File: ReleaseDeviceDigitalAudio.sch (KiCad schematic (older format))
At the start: 7 parts, among them J1 Conn_02x08_Counter_Clockwise

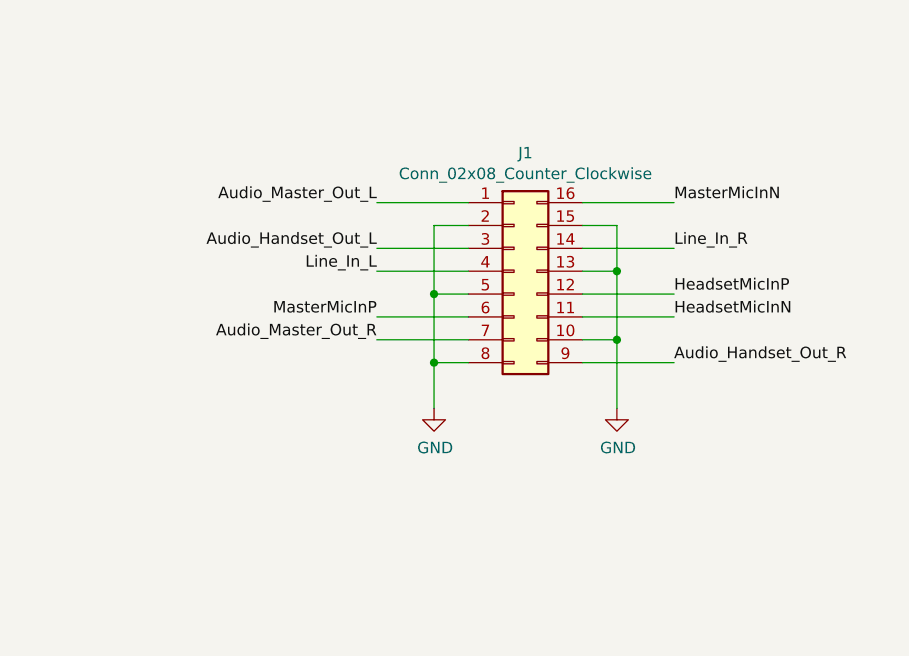
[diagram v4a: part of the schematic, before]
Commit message: - auf 20pol Audiostecker umgebaut
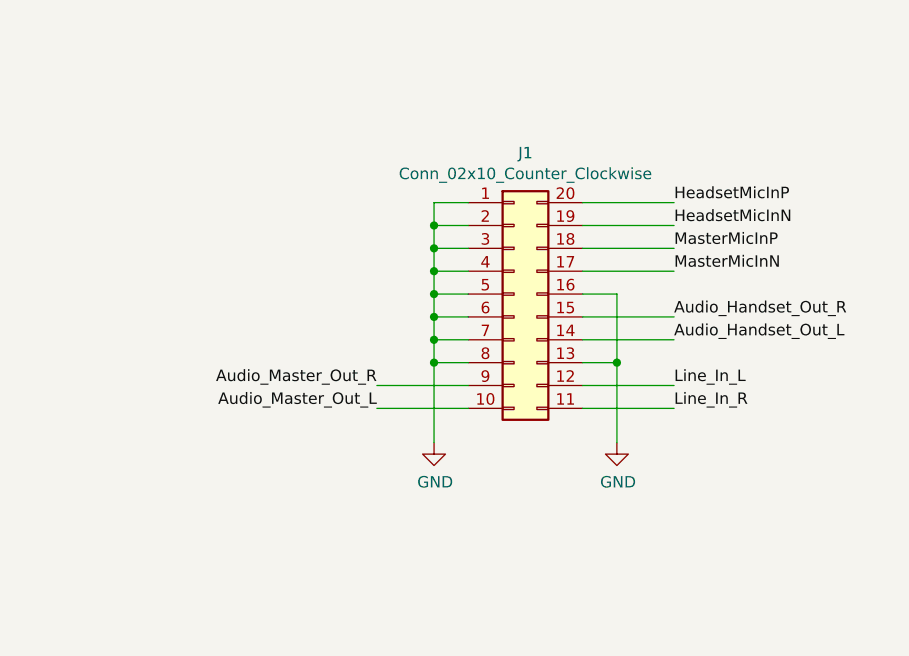
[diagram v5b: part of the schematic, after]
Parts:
- removed J1: Conn_02x08_Counter_Clockwise, TeKaDe:Molex_34825-0160, symbol Connector_Generic:Conn_02x08_Counter_Clockwise
- added J1: Conn_02x10_Counter_Clockwise, TeKaDe:Molex_34825-0200, symbol Connector_Generic:Conn_02x10_Counter_Clockwise
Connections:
- net Audio_Handset_Out_L: now also J1.14 (Pin_14)
- net Audio_Handset_Out_R: now also J1.15 (Pin_15)
- net Audio_Master_Out_L: now also J1.10 (Pin_10)
- net Audio_Master_Out_R: now also J1.9 (Pin_9)
- net GND: now also J1.1 (Pin_1), J1.13 (Pin_13), J1.16 (Pin_16), J1.2 (Pin_2), J1.3 (Pin_3), J1.4 (Pin_4), J1.5 (Pin_5), J1.6 (Pin_6), J1.7 (Pin_7), J1.8 (Pin_8)
- net HeadsetMicInN: now also J1.19 (Pin_19)
- net HeadsetMicInP: now also J1.20 (Pin_20)
- net Line_In_L: now also J1.12 (Pin_12)
- net Line_In_R: now also J1.11 (Pin_11)
- net MasterMicInN: now also J1.17 (Pin_17)
- net MasterMicInP: now also J1.18 (Pin_18)
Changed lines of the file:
@@
 L power:GND #PWR02
 U 1 1 62252CE5
-P 13000 2600
-F 0 "#PWR02" H 13000 2350 50  0001 C CNN
-F 1 "GND" H 13005 2427 50  0000 C CNN
-F 2 "" H 13000 2600 50  0001 C CNN
-F 3 "" H 13000 2600 50  0001 C CNN
-	1    13000 2600
+P 13000 2750
+F 0 "#PWR02" H 13000 2500 50  0001 C CNN
+F 1 "GND" H 13005 2577 50  0000 C CNN
+F 2 "" H 13000 2750 50  0001 C CNN
+F 3 "" H 13000 2750 50  0001 C CNN
+	1    13000 2750
 	1    0    0    -1
 $EndComp
@@
 Wire Wire Line
 	9650 7850 10950 7850
-$Comp
-L Connector_Generic:Conn_02x08_Counter_Clockwise J1
-U 1 1 618DA775
-P 13350 2000
-F 0 "J1" H 13400 2517 50  0000 C CNN
-F 1 "Conn_02x08_Counter_Clockwise" H 13400 2426 50  0000 C CNN
-F 2 "TeKaDe:Molex_34825-0160" H 13350 2000 50  0001 C CNN
-F 3 "~" H 13350 2000 50  0001 C CNN
-	1    13350 2000
-	1    0    0    -1
-$EndComp
 Wire Wire Line
 	9650 2000 10050 2000
@@
 	9650 1350 10050 1350
 Wire Wire Line
-	12750 1700 13150 1700
+	12750 2600 13150 2600
 Wire Wire Line
 	9650 1450 10050 1450
 Wire Wire Line
-	13150 2200 12750 2200
+	13650 1900 14050 1900
+Wire Wire Line
+	13650 1700 14050 1700
+Wire Wire Line
+	13650 2300 14050 2300
+Wire Wire Line
+	13650 2500 14050 2500
+Wire Wire Line
+	13650 2000 14050 2000
+Text Label 14050 2300 0    50   ~ 0
+Audio_Handset_Out_L
+Text Label 14050 2200 0    50   ~ 0
+Audio_Handset_Out_R
+Text Label 14050 1700 0    50   ~ 0
+HeadsetMicInP
+Text Label 12750 2600 2    50   ~ 0
+Audio_Master_Out_L
+Text Label 12750 2500 2    50   ~ 0
+Audio_Master_Out_R
+Text Label 14050 2000 0    50   ~ 0
+MasterMicInN
+Text Label 14050 1900 0    50   ~ 0
+MasterMicInP
+Text Label 14050 2600 0    50   ~ 0
+Line_In_R
+Text Label 14050 2500 0    50   ~ 0
+Line_In_L
+Wire Wire Line
+	13650 2600 14050 2600
+Wire Wire Line
+	13150 2500 12750 2500
 Wire Wire Line
 	13650 2200 14050 2200
-Wire Wire Line
-	13650 2100 14050 2100
-Wire Wire Line
-	13150 1900 12750 1900
-Wire Wire Line
-	13150 2000 12750 2000
-Wire Wire Line
-	13650 1700 14050 1700
-Text Label 12750 1900 2    50   ~ 0
-Audio_Handset_Out_L
-Text Label 14050 2400 0    50   ~ 0
-Audio_Handset_Out_R
-Text Label 14050 2200 0    50   ~ 0
-HeadsetMicInN
-Text Label 14050 2100 0    50   ~ 0
-HeadsetMicInP
-Text Label 12750 1700 2    50   ~ 0
-Audio_Master_Out_L
-Text Label 12750 2300 2    50   ~ 0
-Audio_Master_Out_R
-Text Label 14050 1700 0    50   ~ 0
-MasterMicInN
-Text Label 12750 2200 2    50   ~ 0
-MasterMicInP
-Text Label 14050 1900 0    50   ~ 0
-Line_In_R
-Text Label 12750 2000 2    50   ~ 0
-Line_In_L
-Wire Wire Line
-	13650 1900 14050 1900
-Wire Wire Line
-	13150 2300 12750 2300
-Wire Wire Line
-	13650 2400 14050 2400
-Wire Wire Line
-	13000 1800 13000 2100
+$Comp
+L power:GND #PWR0183
+U 1 1 6194BA95
+P 13800 2750
+F 0 "#PWR0183" H 13800 2500 50  0001 C CNN
+F 1 "GND" H 13805 2577 50  0000 C CNN
+F 2 "" H 13800 2750 50  0001 C CNN
+F 3 "" H 13800 2750 50  0001 C CNN
+	1    13800 2750
+	1    0    0    -1
+$EndComp
+$Comp
+L Connector_Generic:Conn_02x10_Counter_Clockwise J1
+U 1 1 61A33ABF
+P 13350 2100
+F 0 "J1" H 13400 2717 50  0000 C CNN
+F 1 "Conn_02x10_Counter_Clockwise" H 13400 2626 50  0000 C CNN
+F 2 "TeKaDe:Molex_34825-0200" H 13350 2100 50  0001 C CNN
+F 3 "~" H 13350 2100 50  0001 C CNN
+	1    13350 2100
+	1    0    0    -1
+$EndComp
+Wire Wire Line
+	13000 1800 13000 1900
+Wire Wire Line
+	13150 2000 13000 2000
+Connection ~ 13000 2000
+Wire Wire Line
+	13000 2000 13000 2100
+Wire Wire Line
+	13650 2400 13800 2400
+Wire Wire Line
+	13650 2100 13800 2100
+Wire Wire Line
+	13800 2100 13800 2400
+Connection ~ 13800 2400
 Wire Wire Line
 	13150 2100 13000 2100
 Connection ~ 13000 2100
 Wire Wire Line
+	13000 2100 13000 2200
+Wire Wire Line
+	13150 2300 13000 2300
+Connection ~ 13000 2300
+Wire Wire Line
+	13000 2300 13000 2400
+Wire Wire Line
+	13150 1700 13000 1700
+Wire Wire Line
+	13000 1700 13000 1800
+Connection ~ 13000 1800
+Wire Wire Line
+	13800 2400 13800 2750
+Wire Wire Line
+	13150 1900 13000 1900
+Connection ~ 13000 1900
+Wire Wire Line
+	13000 1900 13000 2000
+Text Label 14050 1800 0    50   ~ 0
+HeadsetMicInN
+Wire Wire Line
+	13650 1800 14050 1800
+Wire Wire Line
 	13150 2400 13000 2400
-$Comp
-L power:GND #PWR0183
-U 1 1 6194BA95
-P 13800 2600
-F 0 "#PWR0183" H 13800 2350 50  0001 C CNN
-F 1 "GND" H 13805 2427 50  0000 C CNN
-F 2 "" H 13800 2600 50  0001 C CNN
-F 3 "" H 13800 2600 50  0001 C CNN
-	1    13800 2600
-	1    0    0    -1
-$EndComp
-Wire Wire Line
-	13650 1800 13800 1800
-Wire Wire Line
-	13800 1800 13800 2000
-Wire Wire Line
-	13650 2000 13800 2000
-Wire Wire Line
-	13650 2300 13800 2300
-Connection ~ 13800 2300
-Wire Wire Line
-	13800 2300 13800 2600
 Connection ~ 13000 2400
 Wire Wire Line
-	13000 2400 13000 2600
-Wire Wire Line
-	13000 2100 13000 2400
-Connection ~ 13800 2000
-Wire Wire Line
-	13800 2000 13800 2300
+	13000 2400 13000 2750
+Wire Wire Line
+	13150 2200 13000 2200
+Connection ~ 13000 2200
+Wire Wire Line
+	13000 2200 13000 2300
 $EndSCHEMATC

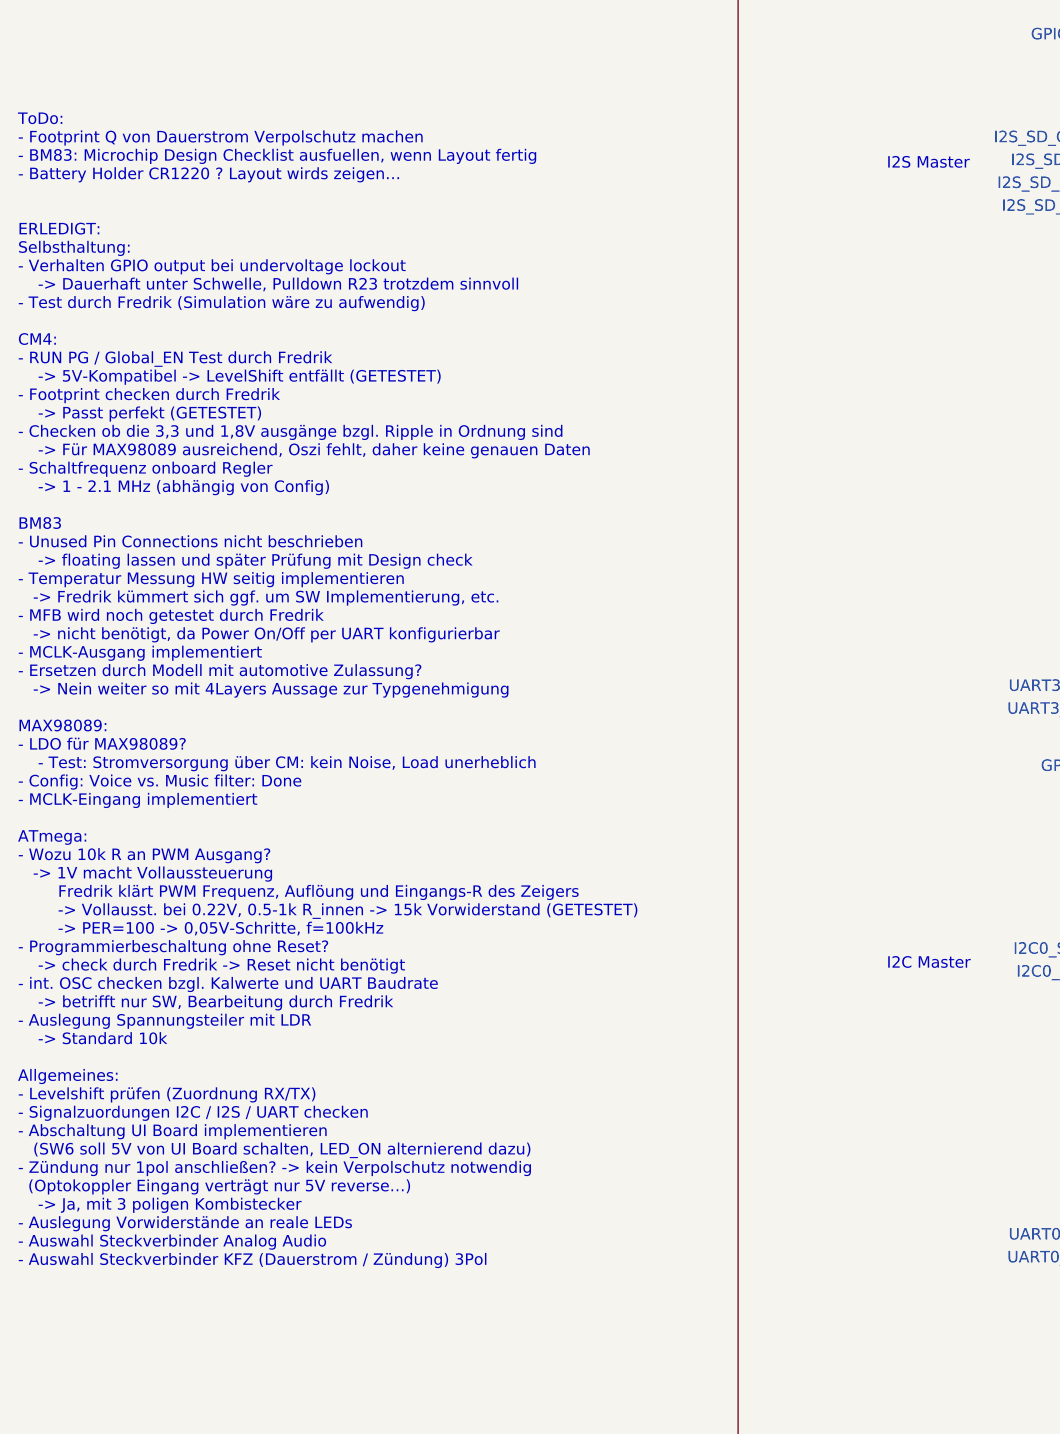
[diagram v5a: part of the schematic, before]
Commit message: - Layout Zwischenstand, UI Board Ansteuerung fast fertig - GPIOs von ATmega komplett umsortiert - Darlington Anschlüsse umsortiert
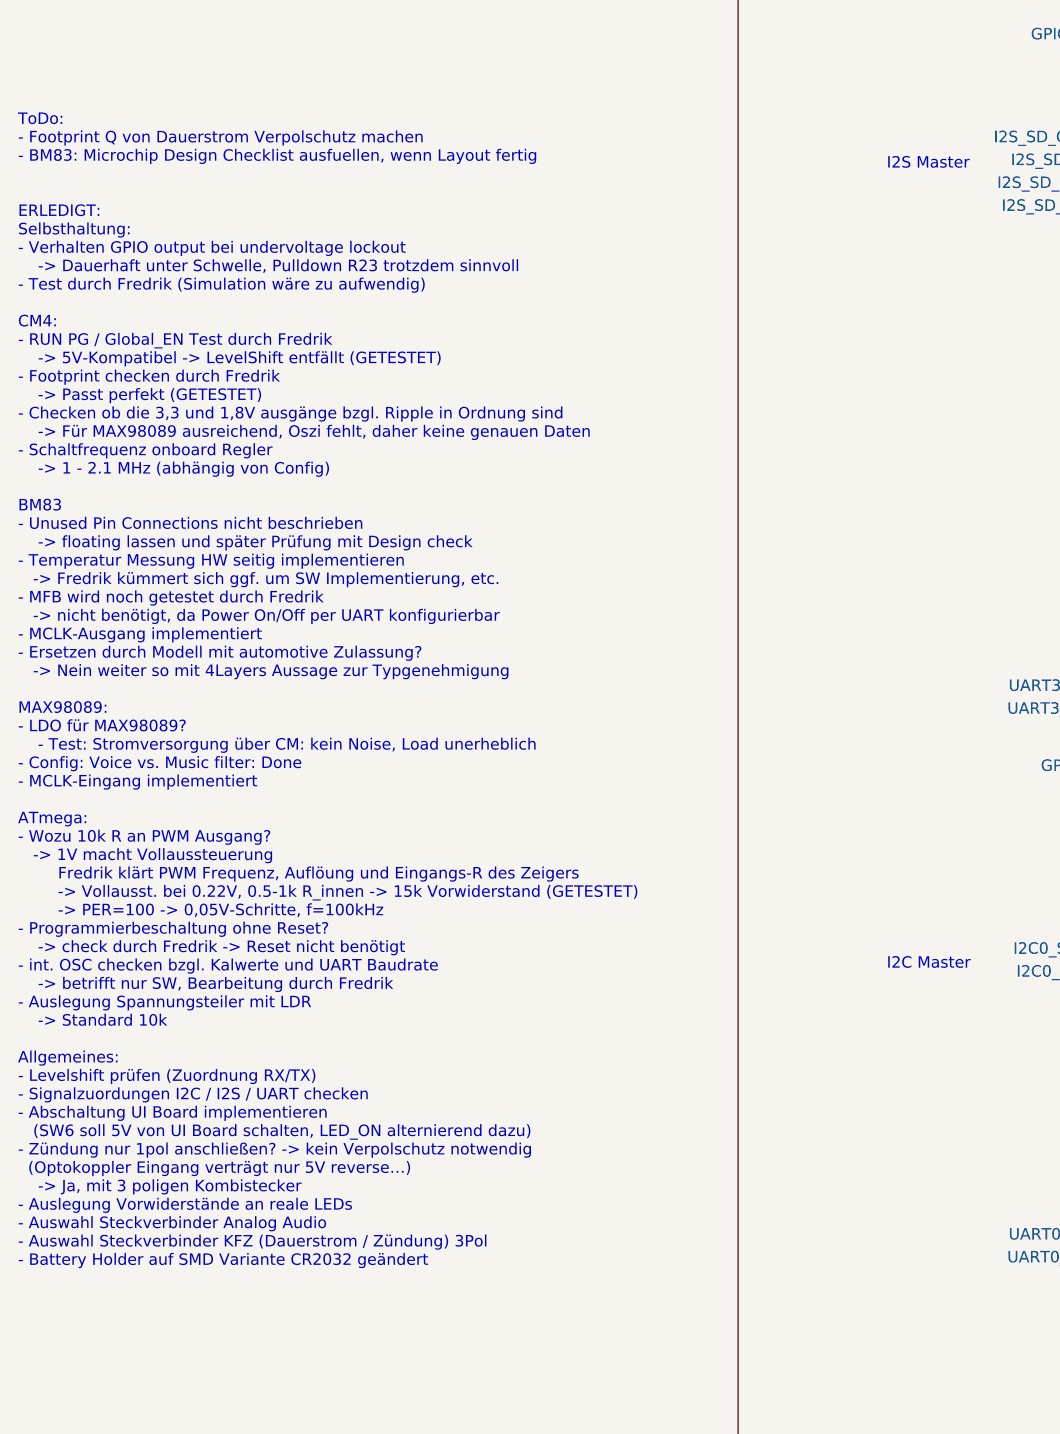
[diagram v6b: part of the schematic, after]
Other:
- note added: "ToDo: \n- Footprint Q von Dauerstrom Verpolschutz machen\n- BM83: Microchip Design Checklist ausfuellen, wenn Layout fertig\n\n\nERLEDIGT:\nSelbsthaltung:\n- Verhalten GPIO output bei undervoltage lockout \n -> Dauerhaft unter Schwelle, Pulldown R23 trotzdem sinnvoll\n- Test durch Fredrik (Simulation wäre zu aufwendig)\n\nCM4: \n- RUN PG / Global_EN Test durch Fredrik\n -> 5V-Kompatibel -> LevelS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"
- note removed: "ToDo: \n- Footprint Q von Dauerstrom Verpolschutz machen\n- BM83: Microchip Design Checklist ausfuellen, wenn Layout fertig\n- Battery Holder CR1220 ? Layout wirds zeigen…\n\n\nERLEDIGT:\nSelbsthaltung:\n- Verhalten GPIO output bei undervoltage lockout \n -> Dauerhaft unter Schwelle, Pulldown R23 trotzdem sinnvoll\n- Test durch Fredrik (Simulation wäre zu aufwendig)\n\nCM4: \n- RUN PG / Global_EN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"
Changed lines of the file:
@@
 $EndComp
 Text Notes 800  7100 0    50   ~ 0
-ToDo: \n- Footprint Q von Dauerstrom Verpolschutz machen\n- BM83: Microchip Design Checklist ausfuellen, wenn Layout fertig\n- Battery Holder CR1220 ? Layout wirds zeigen…\n\n\nERLEDIGT:\nSelbsthaltung:\n- Verhalten GPIO output bei undervoltage lockout \n    -> Dauerhaft unter Schwelle, Pulldown R23 trotzdem sinnvoll\n- Test durch Fredrik (Simulation wäre zu aufwendig)\n\nCM4: \n- RUN PG / Global_EN Test durch Fredrik\n    -> 5V-Kompatibel -> LevelShift entfällt (GETESTET)\n- Footprint checken durch Fredrik\n    -> Passt perfekt (GETESTET)\n- Checken ob die 3,3 und 1,8V ausgänge bzgl. Ripple in Ordnung sind\n    -> Für MAX98089 ausreichend, Oszi fehlt, daher keine genauen Daten\n- Schaltfrequenz onboard Regler\n    -> 1 - 2.1 MHz (abhängig von Config)\n\nBM83\n- Unused Pin Connections nicht beschrieben \n    -> floating lassen und später Prüfung mit Design check\n- Temperatur Messung HW seitig implementieren\n   -> Fredrik kümmert sich ggf. um SW Implementierung, etc.\n- MFB wird noch getestet durch Fredrik  \n   -> nicht benötigt, da Power On/Off per UART konfigurierbar\n- MCLK-Ausgang implementiert\n- Ersetzen durch Modell mit automotive Zulassung?\n   -> Nein weiter so mit 4Layers Aussage zur Typgenehmigung\n\nMAX98089:\n- LDO für MAX98089? \n    - Test: Stromversorgung über CM: kein Noise, Load unerheblich\n- Config: Voice vs. Music filter: Done\n- MCLK-Eingang implementiert\n\nATmega:\n- Wozu 10k R an PWM Ausgang?\n   -> 1V macht Vollaussteuerung\n        Fredrik klärt PWM Frequenz, Auflöung und Eingangs-R des Zeigers\n        -> Vollausst. bei 0.22V, 0.5-1k R_innen -> 15k Vorwiderstand (GETESTET)\n        -> PER=100 -> 0,05V-Schritte, f=100kHz\n- Programmierbeschaltung ohne Reset?\n    -> check durch Fredrik -> Reset nicht benötigt\n- int. OSC checken bzgl. Kalwerte und UART Baudrate\n    -> betrifft nur SW, Bearbeitung durch Fredrik\n- Auslegung Spannungsteiler mit LDR\n    -> Standard 10k\n\nAllgemeines: \n- Levelshift prüfen (Zuordnung RX/TX)\n- Signalzuordungen I2C / I2S / UART checken\n- Abschaltung UI Board implementieren \n   (SW6 soll 5V von UI Board schalten, LED_ON alternierend dazu)\n- Zündung nur 1pol anschließen? -> kein Verpolschutz notwendig\n  (Optokoppler Eingang verträgt nur 5V reverse…)\n    -> Ja, mit 3 poligen Kombistecker\n- Auslegung Vorwiderstände an reale LEDs\n- Auswahl Steckverbinder Analog Audio\n- Auswahl Steckverbinder KFZ (Dauerstrom / Zündung) 3Pol
+ToDo: \n- Footprint Q von Dauerstrom Verpolschutz machen\n- BM83: Microchip Design Checklist ausfuellen, wenn Layout fertig\n\n\nERLEDIGT:\nSelbsthaltung:\n- Verhalten GPIO output bei undervoltage lockout \n    -> Dauerhaft unter Schwelle, Pulldown R23 trotzdem sinnvoll\n- Test durch Fredrik (Simulation wäre zu aufwendig)\n\nCM4: \n- RUN PG / Global_EN Test durch Fredrik\n    -> 5V-Kompatibel -> LevelShift entfällt (GETESTET)\n- Footprint checken durch Fredrik\n    -> Passt perfekt (GETESTET)\n- Checken ob die 3,3 und 1,8V ausgänge bzgl. Ripple in Ordnung sind\n    -> Für MAX98089 ausreichend, Oszi fehlt, daher keine genauen Daten\n- Schaltfrequenz onboard Regler\n    -> 1 - 2.1 MHz (abhängig von Config)\n\nBM83\n- Unused Pin Connections nicht beschrieben \n    -> floating lassen und später Prüfung mit Design check\n- Temperatur Messung HW seitig implementieren\n   -> Fredrik kümmert sich ggf. um SW Implementierung, etc.\n- MFB wird noch getestet durch Fredrik  \n   -> nicht benötigt, da Power On/Off per UART konfigurierbar\n- MCLK-Ausgang implementiert\n- Ersetzen durch Modell mit automotive Zulassung?\n   -> Nein weiter so mit 4Layers Aussage zur Typgenehmigung\n\nMAX98089:\n- LDO für MAX98089? \n    - Test: Stromversorgung über CM: kein Noise, Load unerheblich\n- Config: Voice vs. Music filter: Done\n- MCLK-Eingang implementiert\n\nATmega:\n- Wozu 10k R an PWM Ausgang?\n   -> 1V macht Vollaussteuerung\n        Fredrik klärt PWM Frequenz, Auflöung und Eingangs-R des Zeigers\n        -> Vollausst. bei 0.22V, 0.5-1k R_innen -> 15k Vorwiderstand (GETESTET)\n        -> PER=100 -> 0,05V-Schritte, f=100kHz\n- Programmierbeschaltung ohne Reset?\n    -> check durch Fredrik -> Reset nicht benötigt\n- int. OSC checken bzgl. Kalwerte und UART Baudrate\n    -> betrifft nur SW, Bearbeitung durch Fredrik\n- Auslegung Spannungsteiler mit LDR\n    -> Standard 10k\n\nAllgemeines: \n- Levelshift prüfen (Zuordnung RX/TX)\n- Signalzuordungen I2C / I2S / UART checken\n- Abschaltung UI Board implementieren \n   (SW6 soll 5V von UI Board schalten, LED_ON alternierend dazu)\n- Zündung nur 1pol anschließen? -> kein Verpolschutz notwendig\n  (Optokoppler Eingang verträgt nur 5V reverse…)\n    -> Ja, mit 3 poligen Kombistecker\n- Auslegung Vorwiderstände an reale LEDs\n- Auswahl Steckverbinder Analog Audio\n- Auswahl Steckverbinder KFZ (Dauerstrom / Zündung) 3Pol\n- Battery Holder auf SMD Variante CR2032 geändert
 Wire Wire Line
 	9650 2400 10050 2400

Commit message: - Layout MAX98 - Audiostecker Belegung angepasst
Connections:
- net Audio_Handset_Out_L: now also J1.11 (Pin_11); no longer J1.14 (Pin_14)
- net Audio_Handset_Out_R: now also J1.12 (Pin_12); no longer J1.15 (Pin_15)
- net HeadsetMicInN: now also J1.18 (Pin_18); no longer J1.19 (Pin_19)
- net HeadsetMicInP: now also J1.17 (Pin_17); no longer J1.20 (Pin_20)
- net Line_In_L: now also J1.14 (Pin_14); no longer J1.12 (Pin_12)
- net Line_In_R: now also J1.15 (Pin_15); no longer J1.11 (Pin_11)
- net MasterMicInN: now also J1.20 (Pin_20); no longer J1.17 (Pin_17)
- net MasterMicInP: now also J1.19 (Pin_19); no longer J1.18 (Pin_18)
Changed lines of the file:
@@
 	9650 1450 10050 1450
 Wire Wire Line
-	13650 1900 14050 1900
+	13650 1800 14050 1800
 Wire Wire Line
-	13650 1700 14050 1700
+	13650 2000 14050 2000
+Wire Wire Line
+	13650 2600 14050 2600
 Wire Wire Line
 	13650 2300 14050 2300
 Wire Wire Line
-	13650 2500 14050 2500
-Wire Wire Line
-	13650 2000 14050 2000
-Text Label 14050 2300 0    50   ~ 0
+	13650 1700 14050 1700
+Text Label 14050 2600 0    50   ~ 0
 Audio_Handset_Out_L
-Text Label 14050 2200 0    50   ~ 0
+Text Label 14050 2500 0    50   ~ 0
 Audio_Handset_Out_R
-Text Label 14050 1700 0    50   ~ 0
+Text Label 14050 2000 0    50   ~ 0
 HeadsetMicInP
 Text Label 12750 2600 2    50   ~ 0
@@
 Text Label 12750 2500 2    50   ~ 0
 Audio_Master_Out_R
-Text Label 14050 2000 0    50   ~ 0
+Text Label 14050 1700 0    50   ~ 0
 MasterMicInN
-Text Label 14050 1900 0    50   ~ 0
+Text Label 14050 1800 0    50   ~ 0
 MasterMicInP
-Text Label 14050 2600 0    50   ~ 0
+Text Label 14050 2200 0    50   ~ 0
 Line_In_R
-Text Label 14050 2500 0    50   ~ 0
+Text Label 14050 2300 0    50   ~ 0
 Line_In_L
 Wire Wire Line
-	13650 2600 14050 2600
+	13650 2200 14050 2200
 Wire Wire Line
 	13150 2500 12750 2500
 Wire Wire Line
-	13650 2200 14050 2200
+	13650 2500 14050 2500
 $Comp
 L power:GND #PWR0183
@@
 Wire Wire Line
 	13000 1900 13000 2000
-Text Label 14050 1800 0    50   ~ 0
+Text Label 14050 1900 0    50   ~ 0
 HeadsetMicInN
 Wire Wire Line
-	13650 1800 14050 1800
+	13650 1900 14050 1900
 Wire Wire Line
 	13150 2400 13000 2400
